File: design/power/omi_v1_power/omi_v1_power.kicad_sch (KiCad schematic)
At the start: 9 parts

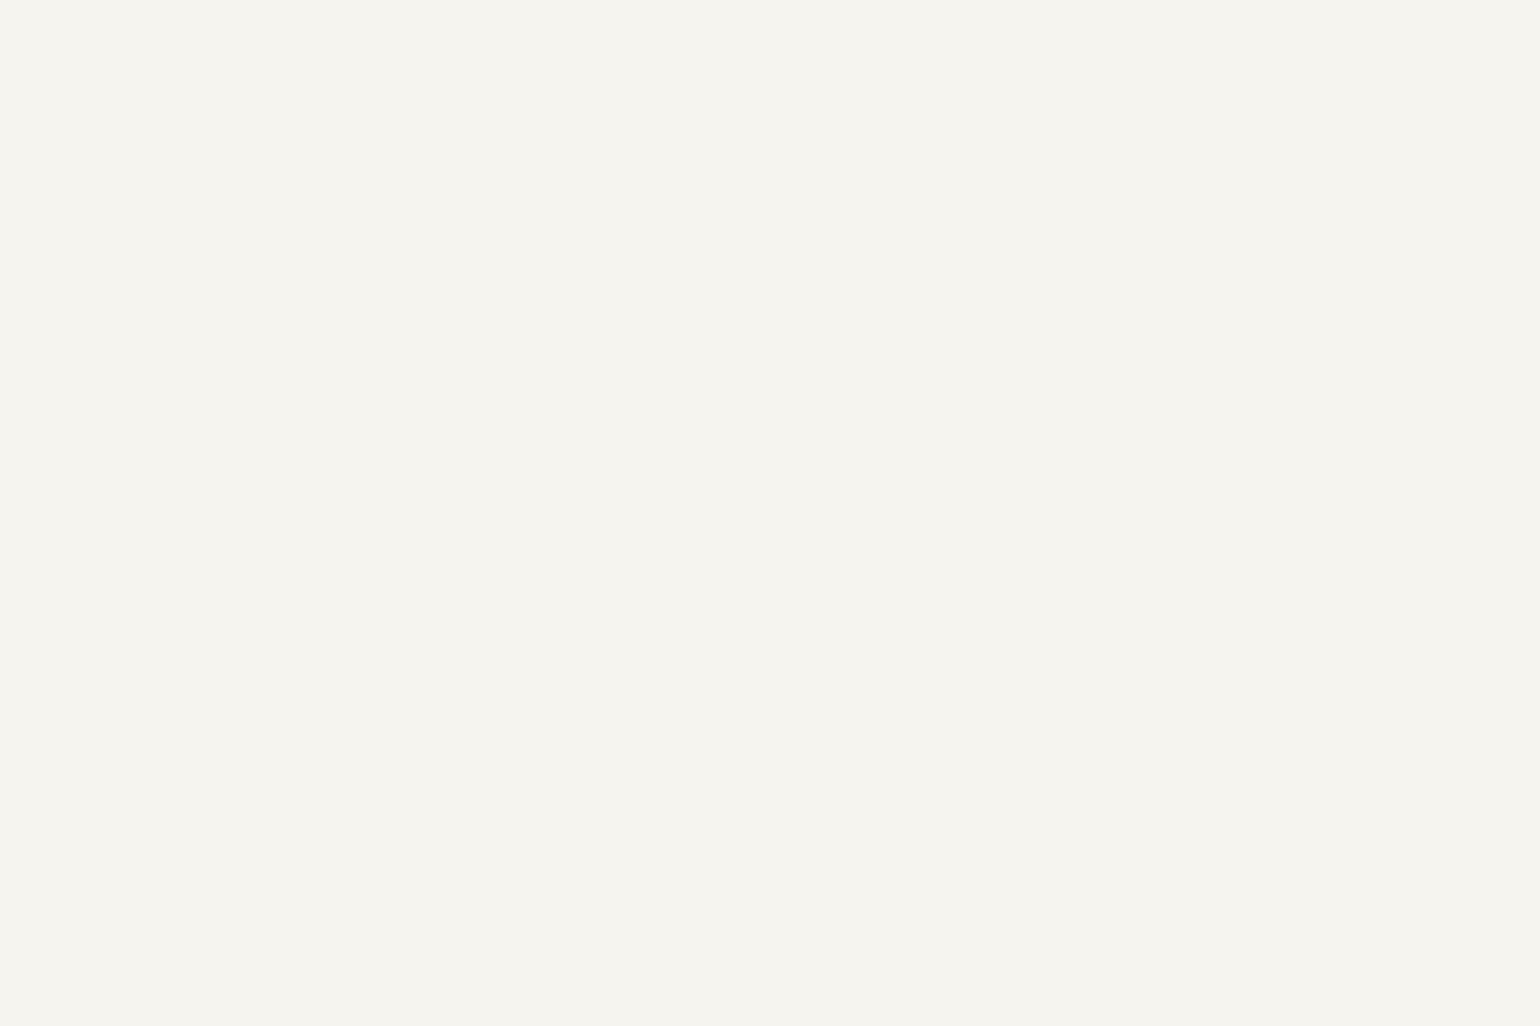
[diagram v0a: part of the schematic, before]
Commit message: feat: Initialize KiCad project for omi_v1_power, including main and address-command-clock schematics.
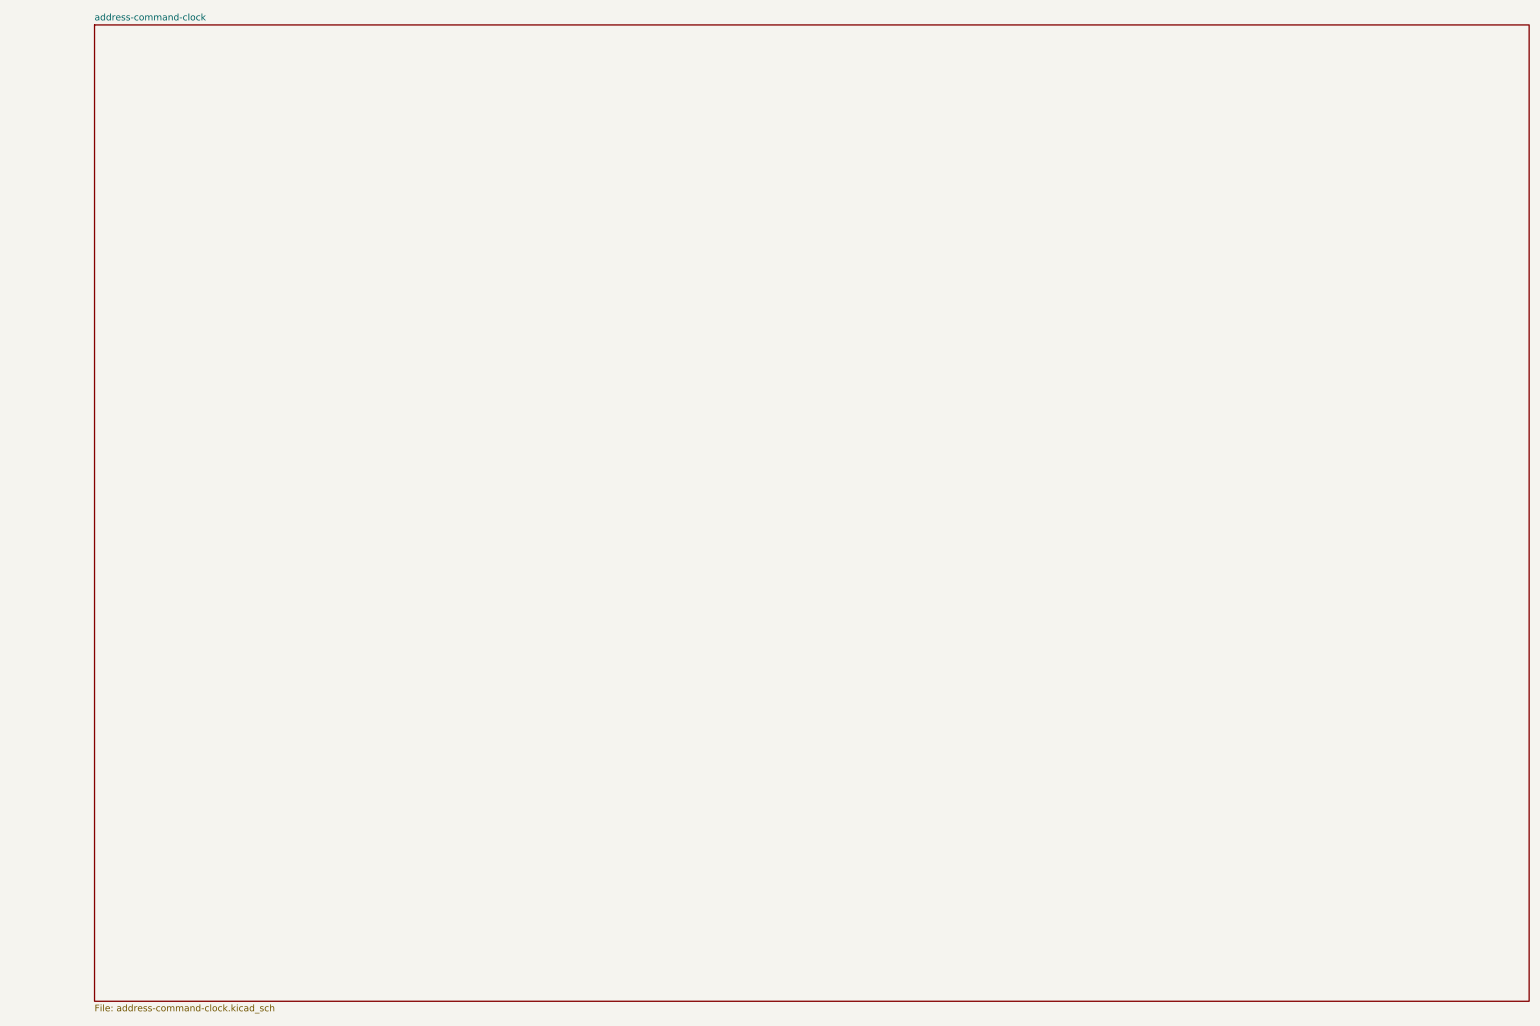
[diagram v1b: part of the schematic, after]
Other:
- added sheet address-command-clock (address-command-clock.kicad_sch)
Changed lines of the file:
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@@
+		)
+	)
+	(sheet
+		(at 370.84 0)
+		(size 274.32 186.69)
+		(exclude_from_sim no)
+		(in_bom yes)
+		(on_board yes)
+		(dnp no)
+		(fields_autoplaced yes)
+		(stroke
+			(width 0.1524)
+			(type solid)
+		)
+		(fill
+			(color 0 0 0 0.0000)
+		)
+		(property "Sheetname" "address-command-clock"
+			(at 370.84 -0.7116 0)
+			(effects
+				(font
+					(size 1.27 1.27)
+				)
+				(justify left bottom)
+			)
+		)
+		(property "Sheetfile" "address-command-clock.kicad_sch"
+			(at 370.84 187.2746 0)
+			(effects
+				(font
+					(size 1.27 1.27)
+				)
+				(justify left top)
+			)
+		)
+		(instances
+			(project "omi_v1_power"
+				(path "/464309c0-e3ad-4428-a43f-e1cf3b7a7d42"
+					(page "2")
+				)
+			)
 		)
 	)

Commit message: feat: Add OMI v1 Stage 7.2 CA/CLK checkpoint 01 documentation and PDF artifact.
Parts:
- removed U_DRAM0, U_DRAM1, U_DRAM2, U_DRAM3, U_DRAM4, U_DRAM5, U_DRAM6, U_DRAM7: H5AN8G8NAFR-UHC, Package_BGA:FBGA-78_7.5x11mm_Layout2x3x13_P0.8mm, symbol Memory_RAM:H5AN8G8NAFR-UHC
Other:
- moved on the sheet: J_PWR

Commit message: feat: Add OMI v1 Stage 7.3 DQ/DQS documentation and PDF artifact.
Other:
- added sheet data-byte-lanes-dqs (data-byte-lanes-dqs.kicad_sch)
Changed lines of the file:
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@@
+	)
+	(sheet
+		(at 308.61 135.89)
+		(size 39.37 33.02)
+		(exclude_from_sim no)
+		(in_bom yes)
+		(on_board yes)
+		(dnp no)
+		(fields_autoplaced yes)
+		(stroke
+			(width 0.1524)
+			(type solid)
+		)
+		(fill
+			(color 0 0 0 0.0000)
+		)
+		(property "Sheetname" "address-command-clock"
+			(at 308.61 135.1784 0)
+			(effects
+				(font
+					(size 1.27 1.27)
+				)
+				(justify left bottom)
+			)
+		)
+		(property "Sheetfile" "address-command-clock.kicad_sch"
+			(at 308.61 169.4946 0)
+			(effects
+				(font
+					(size 1.27 1.27)
+				)
+				(justify left top)
+			)
+		)
+		(instances
+			(project "omi_v1_power"
+				(path "/464309c0-e3ad-4428-a43f-e1cf3b7a7d42"
+					(page "2")
+				)
+			)
+		)
 	)
 	(sheet
@@
 			(color 0 0 0 0.0000)
 		)
-		(property "Sheetname" "address-command-clock"
+		(property "Sheetname" "data-byte-lanes-dqs"
 			(at 308.61 174.5484 0)
 			(effects
@@
 			)
 		)
-		(property "Sheetfile" "address-command-clock.kicad_sch"
+		(property "Sheetfile" "data-byte-lanes-dqs.kicad_sch"
 			(at 308.61 208.8646 0)
 			(effects
@@
 			(project "omi_v1_power"
 				(path "/464309c0-e3ad-4428-a43f-e1cf3b7a7d42"
-					(page "2")
+					(page "3")
 				)
 			)

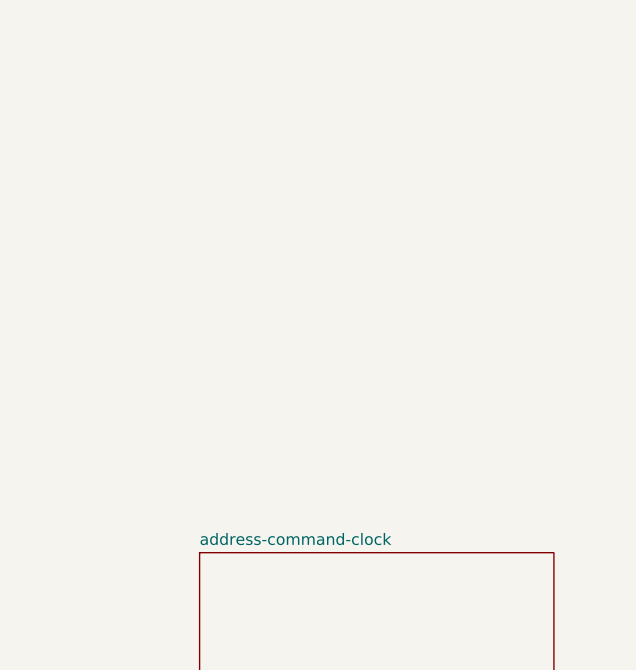
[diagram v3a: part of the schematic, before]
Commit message: feat: Implement OMI v1 power SPD and configuration schematic with accompanying documentation.
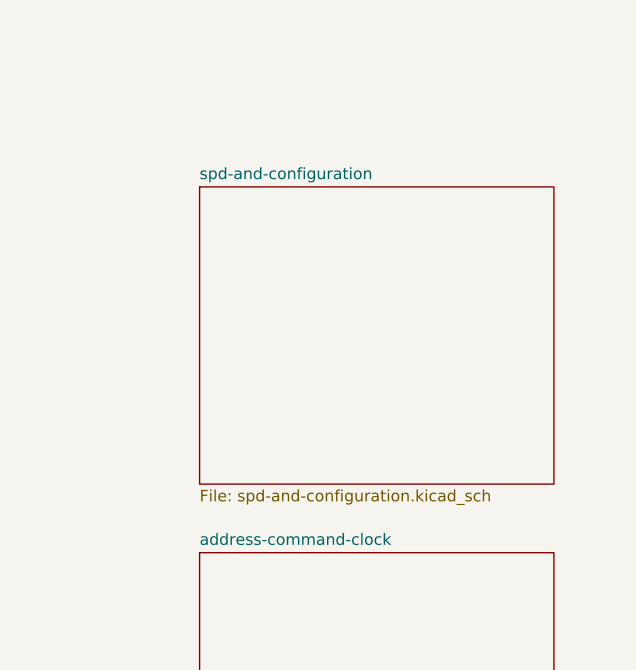
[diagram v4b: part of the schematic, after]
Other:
- added sheet spd-and-configuration (spd-and-configuration.kicad_sch)
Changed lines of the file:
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@@
+	)
+	(sheet
+		(at 308.61 95.25)
+		(size 39.37 33.02)
+		(exclude_from_sim no)
+		(in_bom yes)
+		(on_board yes)
+		(dnp no)
+		(fields_autoplaced yes)
+		(stroke
+			(width 0.1524)
+			(type solid)
+		)
+		(fill
+			(color 0 0 0 0.0000)
+		)
+		(property "Sheetname" "spd-and-configuration"
+			(at 308.61 94.5384 0)
+			(effects
+				(font
+					(size 1.27 1.27)
+				)
+				(justify left bottom)
+			)
+		)
+		(property "Sheetfile" "spd-and-configuration.kicad_sch"
+			(at 308.61 128.8546 0)
+			(effects
+				(font
+					(size 1.27 1.27)
+				)
+				(justify left top)
+			)
+		)
+		(instances
+			(project "omi_v1_power"
+				(path "/464309c0-e3ad-4428-a43f-e1cf3b7a7d42"
+					(page "4")
+				)
+			)
+		)
 	)
 	(sheet

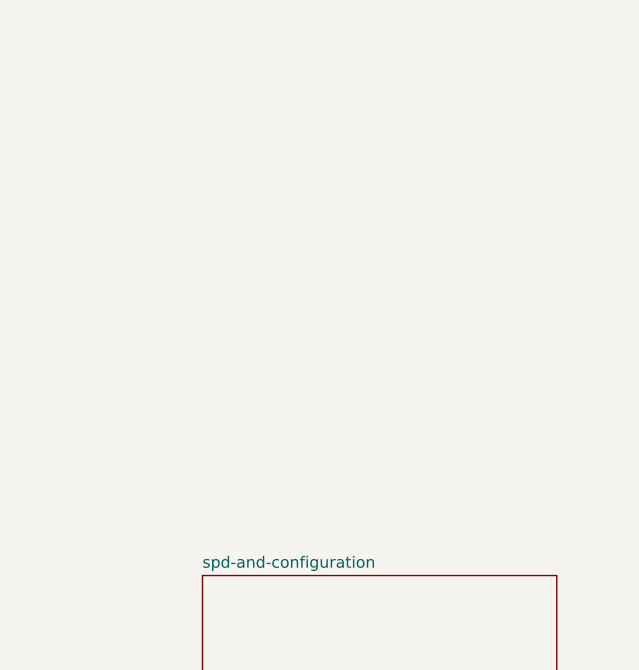
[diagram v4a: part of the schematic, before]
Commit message: feat: Add initial KiCad power schematic, related sub-schematics, and documentation for schematic capture stage 7.
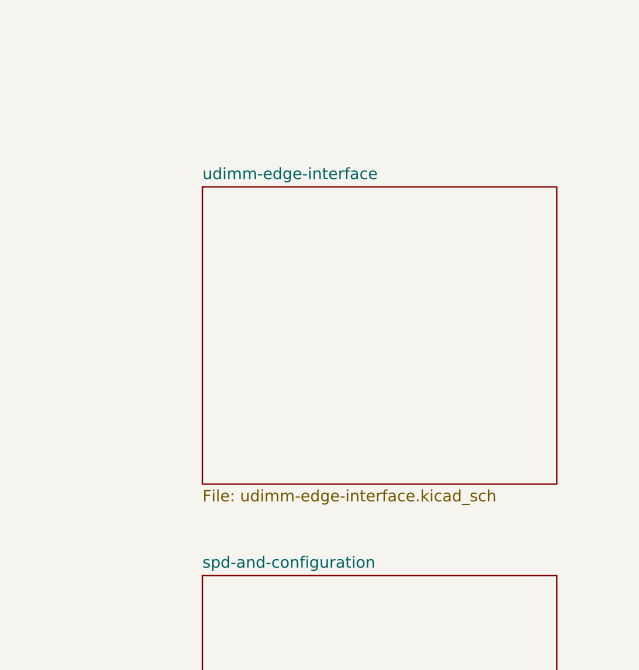
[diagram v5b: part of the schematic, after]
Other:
- added sheet udimm-edge-interface (udimm-edge-interface.kicad_sch)
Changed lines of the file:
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@@
+	)
+	(sheet
+		(at 308.61 52.07)
+		(size 39.37 33.02)
+		(exclude_from_sim no)
+		(in_bom yes)
+		(on_board yes)
+		(dnp no)
+		(fields_autoplaced yes)
+		(stroke
+			(width 0.1524)
+			(type solid)
+		)
+		(fill
+			(color 0 0 0 0.0000)
+		)
+		(property "Sheetname" "udimm-edge-interface"
+			(at 308.61 51.3584 0)
+			(effects
+				(font
+					(size 1.27 1.27)
+				)
+				(justify left bottom)
+			)
+		)
+		(property "Sheetfile" "udimm-edge-interface.kicad_sch"
+			(at 308.61 85.6746 0)
+			(effects
+				(font
+					(size 1.27 1.27)
+				)
+				(justify left top)
+			)
+		)
+		(instances
+			(project "omi_v1_power"
+				(path "/464309c0-e3ad-4428-a43f-e1cf3b7a7d42"
+					(page "5")
+				)
+			)
+		)
 	)
 	(sheet
